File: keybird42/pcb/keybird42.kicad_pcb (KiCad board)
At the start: 2 copper layers, 420.3 x 95.2 mm, 176 parts, among them SW111 SW_MX, SW112 SW_MX, SW113 SW_MX, SW114 SW_MX, SW115 SW_MX, SW116 SW_MX, SW117 SW_MX, SW121 SW_MX, SW122 SW_MX, SW123 SW_MX, SW124 SW_MX, SW125 SW_MX, SW126 SW_MX, SW127 SW_MX, SW131 SW_MX, SW132 SW_MX, SW133 SW_MX, SW134 SW_MX, SW135 SW_MX, SW136 SW_MX, SW137 SW_MX, SW211 SW_MX, SW212 SW_MX, SW213 SW_MX, SW214 SW_MX, SW215 SW_MX, SW216 SW_MX, SW217 SW_MX, SW221 SW_MX, SW222 SW_MX, SW223 SW_MX, SW225 SW_MX, SW226 SW_MX, SW227 SW_MX, SW231 SW_MX, SW232 SW_MX, SW233 SW_MX, SW234 SW_MX, SW235 SW_MX, SW236 SW_MX, SW237 SW_MX, SW311 SW_MX, SW312 SW_MX, SW314 SW_MX, SW315 SW_MX, SW316 SW_MX, SW317 SW_MX, SW321 SW_MX, SW322 SW_MX, SW323 SW_MX, SW324 SW_MX, SW325 SW_MX, SW327 SW_MX, SW331 SW_MX, SW332 SW_MX, SW333 SW_MX, SW334 SW_MX, SW335 SW_MX, SW336 SW_MX, SW337 SW_MX, SW411 SW_MX, SW412 SW_MX, SW413 SW_MX, SW414 SW_MX, SW415 SW_MX, SW416 SW_MX, SW417 SW_MX, SW421 SW_MX, SW423 SW_MX, SW424 SW_MX, SW425 SW_MX, SW426 SW_MX, SW427 SW_MX, SW431 SW_MX, SW432 SW_MX, SW433 SW_MX, SW434 SW_MX, SW436 SW_MX, SW437 SW_MX, SW501 SW_MX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

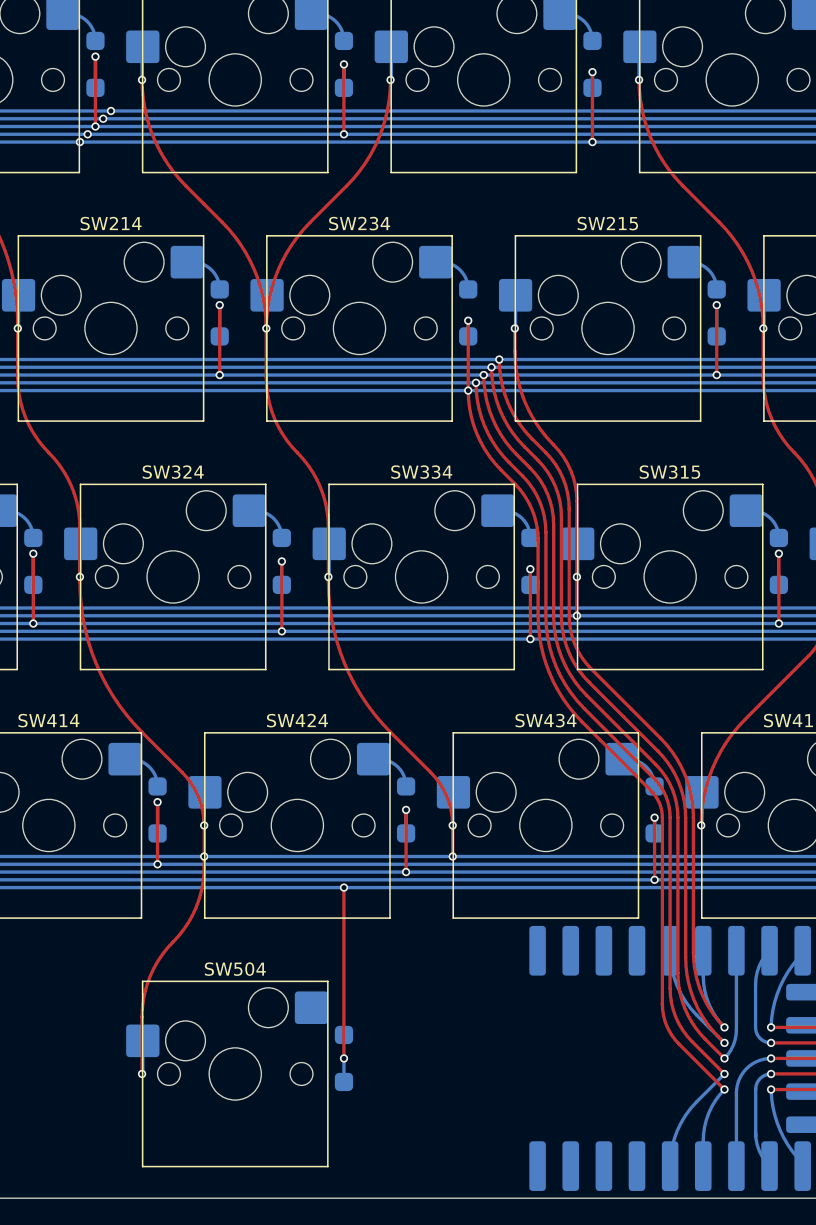
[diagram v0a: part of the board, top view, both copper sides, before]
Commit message: more vertical bus layout
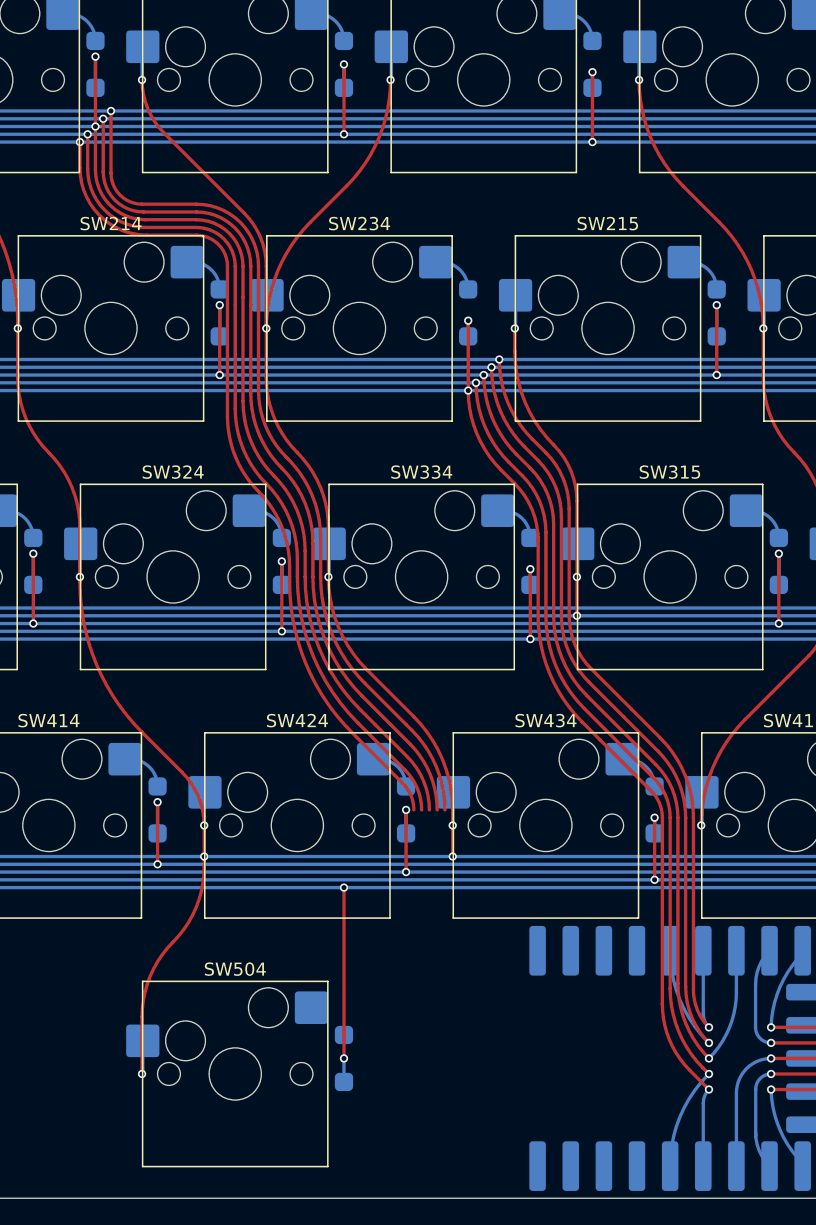
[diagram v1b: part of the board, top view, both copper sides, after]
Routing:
- net /COL1: track 714.5 -> 780.2 mm
- net /COL7: track 661.9 -> 726.9 mm
- net /ROW11: track 464.9 -> 529.3 mm
- net /ROW12: track 460.7 -> 524.5 mm
- net /ROW13: track 456.5 -> 519.7 mm
- net /ROW22: track 521.2 -> 519.9 mm
- net /COL6: track 716.6 -> 715.6 mm
- net /ROW23: track 522.9 -> 522.0 mm
- net /COL4: track 683.8 -> 684.4 mm
- net /COL2: track 726.6 -> 726.1 mm

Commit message: routing done?
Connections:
- U1 pad 1: /ROW12 -> /COL1
- U1 pad 17: /ROW23 -> /ROW21
- U1 pad 18: /ROW22 -> /ROW23
- U1 pad 19: /COL7 -> /ROW13
- U1 pad 2: /ROW13 -> /COL7
- U1 pad 3: /ROW21 -> /ROW12
- U1 pad 4: /COL6 -> /ROW22
- U1 pad 5: /COL2 -> /COL6
- U1 pad 6: /ROW21 -> /COL2
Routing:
- net /ROW12: track 524.5 -> 561.8 mm, vias 15 -> 16
- net /ROW13: track 519.7 -> 556.1 mm, vias 15 -> 16
- net /ROW11: track 529.3 -> 563.8 mm, vias 14 -> 15
- net /COL7: track 726.9 -> 758.2 mm, vias 17 -> 18
- net /COL1: track 780.2 -> 808.7 mm, vias 15 -> 16
- net /COL2: track 726.1 -> 729.6 mm
- net /ROW21: track 531.4 -> 530.8 mm

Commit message: starting to fix DRC complaints
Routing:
- net /COL4: track 684.4 -> 679.6 mm
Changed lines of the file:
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@@
   (segment (start 226.21894 88.106324) (end 226.21894 88.905917) (width 0.254) (layer "F.Cu") (net 103))
   (segment (start 221.456436 100.403617) (end 221.456436 104.775088) (width 0.254) (layer "F.Cu") (net 103))
+  (segment (start 226.21894 35.71878) (end 229.718594 39.218434) (width 0.254) (layer "F.Cu") (net 103))
   (segment (start 197.643916 66.675056) (end 197.643916 67.083615) (width 0.254) (layer "F.Cu") (net 103))
-  (segment (start 237.138853 36.705127) (end 234.349043 39.494937) (width 0.254) (layer "F.Cu") (net 103))
+  (segment (start 223.140235 32.640076) (end 226.21894 35.71878) (width 0.254) (layer "F.Cu") (net 103))
   (segment (start 204.090219 32.640076) (end 207.168924 35.71878) (width 0.254) (layer "F.Cu") (net 103))
+  (segment (start 230.981444 42.267223) (end 230.981444 47.62504) (width 0.254) (layer "F.Cu") (net 103))
+  (segment (start 235.743948 35.71878) (end 232.244294 39.218434) (width 0.254) (layer "F.Cu") (net 103))
   (segment (start 226.21894 85.725072) (end 226.21894 88.106324) (width 0.254) (layer "F.Cu") (net 103))
   (segment (start 235.743948 62.898594) (end 235.743948 66.675056) (width 0.254) (layer "F.Cu") (net 103))
-  (segment (start 230.981444 42.862536) (end 230.981444 47.62504) (width 0.254) (layer "F.Cu") (net 103))
   (segment (start 216.693932 62.898898) (end 216.693932 66.675056) (width 0.254) (layer "F.Cu") (net 103))
   (segment (start 221.456436 78.581316) (end 224.53514 81.66002) (width 0.254) (layer "F.Cu") (net 103))
-  (segment (start 226.21894 35.71878) (end 229.297644 38.797484) (width 0.254) (layer "F.Cu") (net 103))
+  (segment (start 238.822653 32.640076) (end 235.743948 35.71878) (width 0.254) (layer "F.Cu") (net 103))
   (segment (start 211.931428 47.62504) (end 211.931428 51.401198) (width 0.254) (layer "F.Cu") (net 103))
-  (segment (start 223.140235 32.640076) (end 226.21894 35.71878) (width 0.254) (layer "F.Cu") (net 103))
   (segment (start 238.690597 73.788896) (end 242.292391 77.39069) (width 0.254) (layer "F.Cu") (net 103))
   (via (at 216.693932 66.675056) (size 0.635) (drill 0.381) (layers "F.Cu" "B.Cu") (net 103))
@@
   (via (at 245.268956 85.725072) (size 0.635) (drill 0.381) (layers "F.Cu" "B.Cu") (net 103))
   (arc (start 207.168924 35.71878) (mid 210.693693 40.99397) (end 211.931428 47.216481) (width 0.254) (layer "F.Cu") (net 103))
-  (arc (start 240.506452 28.575024) (mid 239.631242 32.975004) (end 237.138853 36.705127) (width 0.254) (layer "F.Cu") (net 103))
+  (arc (start 229.718594 39.218434) (mid 230.653239 40.61723) (end 230.981444 42.267223) (width 0.254) (layer "F.Cu") (net 103))
   (arc (start 233.362696 57.150048) (mid 235.125102 59.787537) (end 235.743948 62.898594) (width 0.254) (layer "F.Cu") (net 103))
   (arc (start 242.292391 77.39069) (mid 244.495371 80.687684) (end 245.268956 84.576753) (width 0.254) (layer "F.Cu") (net 103))
   (arc (start 205.485124 81.66002) (mid 206.731319 83.525081) (end 207.168924 85.725072) (width 0.254) (layer "F.Cu") (net 103))
-  (arc (start 221.456436 28.575024) (mid 221.894041 30.775014) (end 223.140235 32.640076) (width 0.254) (layer "F.Cu") (net 103))
   (arc (start 214.31268 57.150048) (mid 216.075065 59.787642) (end 216.693932 62.898898) (width 0.254) (layer "F.Cu") (net 103))
-  (arc (start 234.349043 39.494937) (mid 231.856654 43.22506) (end 230.981444 47.62504) (width 0.254) (layer "F.Cu") (net 103))
   (arc (start 226.21894 88.905917) (mid 225.600073 92.017172) (end 223.837688 94.654767) (width 0.254) (layer "F.Cu") (net 103))
   (arc (start 223.837688 94.654767) (mid 222.075303 97.292361) (end 221.456436 100.403617) (width 0.254) (layer "F.Cu") (net 103))
   (arc (start 224.53514 81.66002) (mid 225.781335 83.525081) (end 226.21894 85.725072) (width 0.254) (layer "F.Cu") (net 103))
   (arc (start 202.40642 28.575024) (mid 202.844025 30.775014) (end 204.090219 32.640076) (width 0.254) (layer "F.Cu") (net 103))
-  (arc (start 229.297644 38.797484) (mid 230.543839 40.662545) (end 230.981444 42.862536) (width 0.254) (layer "F.Cu") (net 103))
   (arc (start 216.693932 67.083615) (mid 217.931666 73.306126) (end 221.456436 78.581316) (width 0.254) (layer "F.Cu") (net 103))
+  (arc (start 240.506452 28.575024) (mid 240.068847 30.775014) (end 238.822653 32.640076) (width 0.254) (layer "F.Cu") (net 103))
+  (arc (start 221.456436 28.575024) (mid 221.894041 30.775014) (end 223.140235 32.640076) (width 0.254) (layer "F.Cu") (net 103))
   (arc (start 230.981444 51.401198) (mid 231.600311 54.512453) (end 233.362696 57.150048) (width 0.254) (layer "F.Cu") (net 103))
   (arc (start 235.743948 66.675056) (mid 236.509757 70.525038) (end 238.690597 73.788896) (width 0.254) (layer "F.Cu") (net 103))
   (arc (start 211.931428 51.401198) (mid 212.550295 54.512453) (end 214.31268 57.150048) (width 0.254) (layer "F.Cu") (net 103))
+  (arc (start 232.244294 39.218434) (mid 231.309648 40.61723) (end 230.981444 42.267223) (width 0.254) (layer "F.Cu") (net 103))
   (arc (start 197.643916 67.083615) (mid 198.88165 73.306126) (end 202.40642 78.581316) (width 0.254) (layer "F.Cu") (net 103))
   (segment (start 207.22768 83.185072) (end 207.22768 85.666316) (width 0.254) (layer "B.Cu") (net 103))
@@
   (arc (start 377.428442 97.631332) (mid 375.778449 97.303128) (end 374.379653 96.368482) (width 0.254) (layer "B.Cu") (net 103))
   (arc (start 207.22768 85.666316) (mid 207.210471 85.707863) (end 207.168924 85.725072) (width 0.254) (layer "B.Cu") (net 103))
-  (arc (start 230.981444 45.226366) (mid 230.996662 45.14986) (end 231.04 45.085) (width 0.254) (layer "B.Cu") (net 103))
   (segment (start 297.686416 78.611232) (end 296.261595 77.186411) (width 0.254) (layer "F.Cu") (net 104))
   (segment (start 288.131492 47.62504) (end 288.131492 52.83841) (width 0.254) (layer "F.Cu") (net 104))

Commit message: reduce silkscreen clutter
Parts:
- removed REF** (x2): Stabilizer_Cherry_MX_2.00u, PCM_Mounting_Keyboard_Stabilizer:Stabilizer_Cherry_MX_2.00u
- removed REF**: Stabilizer_Cherry_MX_7.00u, PCM_Mounting_Keyboard_Stabilizer:Stabilizer_Cherry_MX_7.00u
- SW111, SW112, SW113, SW114, SW115, SW116, SW117, SW121, SW122, SW123, SW124, SW125, SW126, SW127, SW131, SW132, SW133, SW134, SW135, SW136, SW137, SW211, SW212, SW213, SW214, SW215, SW216, SW217, SW221, SW222, SW223, SW225, SW226, SW227, SW231, SW232, SW233, SW234, SW235, SW236, SW237, SW311, SW312, SW314, SW315, SW316, SW317, SW321, SW322, SW323, SW324, SW325, SW327, SW331, SW332, SW333, SW334, SW335, SW336, SW337, SW411, SW412, SW413, SW414, SW415, SW416, SW417, SW421, SW423, SW424, SW425, SW426, SW427, SW431, SW432, SW433, SW434, SW436, SW437, SW501, SW502, SW503, SW504, SW505, SW506, SW507: footprint PCM_Switch_Keyboard_Hotswap_Kailh:SW_Hotswap_Kailh_MX -> keybird42:SW_Hotswap_Kailh_MX
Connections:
- U1 pad 1: /COL1 -> /ROW12
- U1 pad 10: /ROW41 -> /ROW42
- U1 pad 11: /ROW42 -> /ROW43
- U1 pad 12: /ROW43 -> /ROW50
- U1 pad 13: /ROW50 -> /COL1
- U1 pad 14: /COL3 -> /COL2
- U1 pad 15: /COL5 -> /COL3
- U1 pad 16: /ROW31 -> /COL4
- U1 pad 17: /ROW21 -> /COL5
- U1 pad 18: /ROW23 -> /COL6
- U1 pad 19: /ROW13 -> /COL7
- U1 pad 2: /COL7 -> /ROW13
- U1 pad 3: /ROW12 -> /ROW21
- U1 pad 5: /COL6 -> /ROW23
- U1 pad 6: /COL2 -> /ROW31
- U1 pad 9: /COL4 -> /ROW41

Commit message: whoops, lost the stabs
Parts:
- added REF**: Stabilizer_Cherry_MX_7.00u, PCM_Mounting_Keyboard_Stabilizer:Stabilizer_Cherry_MX_7.00u, F.Cu at (228.6, 104.8)
- added REF**: Stabilizer_Cherry_MX_2.00u, PCM_Mounting_Keyboard_Stabilizer:Stabilizer_Cherry_MX_2.00u, F.Cu at (107.2, 85.7)
- added REF**: Stabilizer_Cherry_MX_2.00u, PCM_Mounting_Keyboard_Stabilizer:Stabilizer_Cherry_MX_2.00u, F.Cu at (350.0, 66.7)
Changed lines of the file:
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@@
     )
   )
+  (footprint "PCM_Mounting_Keyboard_Stabilizer:Stabilizer_Cherry_MX_7.00u" (layer "F.Cu")
+    (at 228.600192 104.775088 180)
+    (descr "Cherry MX PCB Stabilizer 7.00u")
+    (tags "Cherry MX Keyboard Stabilizer 7.00u Cutout")
+    (attr exclude_from_pos_files exclude_from_bom)
+    (fp_text reference "REF**" (at 0 -3.4) (layer "F.Fab") hide
+        (effects (font (size 1 1) (thickness 0.15)))
+    )
+    (fp_text value "Stabilizer_Cherry_MX_7.00u" (at 0 3.4) (layer "F.Fab") hide
+        (effects (font (size 1 1) (thickness 0.15)))
+    )
+    (fp_line (start -2 0) (end 2 0)
+      (stroke (width 0.1) (type solid)) (layer "Dwgs.User"))
+    (fp_line (start 0 2) (end 0 -2)
+      (stroke (width 0.1) (type solid)) (layer "Dwgs.User"))
+    (fp_line (start -60.525 -5.53) (end -60.525 6.77)
+      (stroke (width 0.1) (type solid)) (layer "Eco1.User"))
+    (fp_line (start -60.525 6.77) (end -53.775 6.77)
+      (stroke (width 0.1) (type solid)) (layer "Eco1.User"))
+    (fp_line (start -53.775 -5.53) (end -60.525 -5.53)
+      (stroke (width 0.1) (type solid)) (layer "Eco1.User"))
+    (fp_line (start -53.775 6.77) (end -53.775 -5.53)
+      (stroke (width 0.1) (type solid)) (layer "Eco1.User"))
+    (fp_line (start 53.775 -5.53) (end 53.775 6.77)
+      (stroke (width 0.1) (type solid)) (layer "Eco1.User"))
+    (fp_line (start 53.775 6.77) (end 60.525 6.77)
+      (stroke (width 0.1) (type solid)) (layer "Eco1.User"))
+    (fp_line (start 60.525 -5.53) (end 53.775 -5.53)
+      (stroke (width 0.1) (type solid)) (layer "Eco1.User"))
+    (fp_line (start 60.525 6.77) (end 60.525 -5.53)
+      (stroke (width 0.1) (type solid)) (layer "Eco1.User"))
+    (pad "" np_thru_hole circle (at -57.15 -6.985 180) (size 3.048 3.048) (drill 3.048) (layers "*.Cu" "*.Mask"))
+    (pad "" np_thru_hole circle (at -57.15 8.225 180) (size 3.9878 3.9878) (drill 3.9878) (layers "*.Cu" "*.Mask"))
+    (pad "" np_thru_hole circle (at 57.15 -6.985 180) (size 3.048 3.048) (drill 3.048) (layers "*.Cu" "*.Mask"))
+    (pad "" np_thru_hole circle (at 57.15 8.225 180) (size 3.9878 3.9878) (drill 3.9878) (layers "*.Cu" "*.Mask"))
+    (model "${KICAD6_3RD_PARTY}/3dmodels/com_github_perigoso_keyswitch-kicad-library/3d-library.3dshapes/Stabilizer_Cherry_MX_7.00u.wrl"
+      (offset (xyz 0 0 0))
+      (scale (xyz 1 1 1))
+      (rotate (xyz 0 0 0))
+    )
+  )
   (footprint "keybird42:SW_Hotswap_Kailh_MX" (layer "F.Cu")
     (at 404.8125 52.3875)
@@
     )
   )
+  (footprint "PCM_Mounting_Keyboard_Stabilizer:Stabilizer_Cherry_MX_2.00u" (layer "F.Cu")
+    (at 107.15634 85.725072 180)
+    (descr "Cherry MX PCB Stabilizer 2.00u 2.25u 2.50u 2.75u")
+    (tags "Cherry MX Keyboard Stabilizer 2.00u 2.25u 2.50u 2.75u Cutout")
+    (attr exclude_from_pos_files exclude_from_bom)
+    (fp_text reference "REF**" (at 0 -3.4) (layer "F.Fab") hide
+        (effects (font (size 1 1) (thickness 0.15)))
+    )
+    (fp_text value "Stabilizer_Cherry_MX_2.00u" (at 0 3.6) (layer "F.Fab") hide
+        (effects (font (size 1 1) (thickness 0.15)))
+    )
+    (fp_line (start -2 0) (end 2 0)
+      (stroke (width 0.1) (type solid)) (layer "Dwgs.User"))
+    (fp_line (start 0 2) (end 0 -2)
+      (stroke (width 0.1) (type solid)) (layer "Dwgs.User"))
+    (fp_line (start -15.313 -5.53) (end -15.313 6.77)
+      (stroke (width 0.1) (type solid)) (layer "Eco1.User"))
+    (fp_line (start -15.313 6.77) (end -8.563 6.77)
+      (stroke (width 0.1) (type solid)) (layer "Eco1.User"))
+    (fp_line (start -8.563 -5.53) (end -15.313 -5.53)
+      (stroke (width 0.1) (type solid)) (layer "Eco1.User"))
+    (fp_line (start -8.563 6.77) (end -8.563 -5.53)
+      (stroke (width 0.1) (type solid)) (layer "Eco1.User"))
+    (fp_line (start 8.563 -5.53) (end 8.563 6.77)
+      (stroke (width 0.1) (type solid)) (layer "Eco1.User"))
+    (fp_line (start 8.563 6.77) (end 15.313 6.77)
+      (stroke (width 0.1) (type solid)) (layer "Eco1.User"))
+    (fp_line (start 15.313 -5.53) (end 8.563 -5.53)
+      (stroke (width 0.1) (type solid)) (layer "Eco1.User"))
+    (fp_line (start 15.313 6.77) (end 15.313 -5.53)
+      (stroke (width 0.1) (type solid)) (layer "Eco1.User"))
+    (pad "" np_thru_hole circle (at -11.938 -6.985 180) (size 3.048 3.048) (drill 3.048) (layers "*.Cu" "*.Mask"))
+    (pad "" np_thru_hole circle (at -11.938 8.225 180) (size 3.9878 3.9878) (drill 3.9878) (layers "*.Cu" "*.Mask"))
+    (pad "" np_thru_hole circle (at 11.938 -6.985 180) (size 3.048 3.048) (drill 3.048) (layers "*.Cu" "*.Mask"))
+    (pad "" np_thru_hole circle (at 11.938 8.225 180) (size 3.9878 3.9878) (drill 3.9878) (layers "*.Cu" "*.Mask"))
+    (model "${KICAD6_3RD_PARTY}/3dmodels/com_github_perigoso_keyswitch-kicad-library/3d-library.3dshapes/Stabilizer_Cherry_MX_2.00u.wrl"
+      (offset (xyz 0 0 0))
+      (scale (xyz 1 1 1))
+      (rotate (xyz 0 0 0))
+    )
+  )
   (footprint "keybird42:SW_Hotswap_Kailh_MX" (layer "F.Cu")
     (at 385.762824 33.3375)
@@
       (net 11 "Net-(D122-A)") (pinfunction "A") (pintype "passive"))
   )
+  (footprint "PCM_Mounting_Keyboard_Stabilizer:Stabilizer_Cherry_MX_2.00u" (layer "F.Cu")
+    (at 350.044044 66.675056 180)
+    (descr "Cherry MX PCB Stabilizer 2.00u 2.25u 2.50u 2.75u")
+    (tags "Cherry MX Keyboard Stabilizer 2.00u 2.25u 2.50u 2.75u Cutout")
+    (attr exclude_from_pos_files exclude_from_bom)
+    (fp_text reference "REF**" (at 0 -3.4) (layer "F.Fab") hide
+        (effects (font (size 1 1) (thickness 0.15)))
+    )
+    (fp_text value "Stabilizer_Cherry_MX_2.00u" (at 0 3.6) (layer "F.Fab") hide
+        (effects (font (size 1 1) (thickness 0.15)))
+    )
+    (fp_line (start -2 0) (end 2 0)
+      (stroke (width 0.1) (type solid)) (layer "Dwgs.User"))
+    (fp_line (start 0 2) (end 0 -2)
+      (stroke (width 0.1) (type solid)) (layer "Dwgs.User"))
+    (fp_line (start -15.313 -5.53) (end -15.313 6.77)
+      (stroke (width 0.1) (type solid)) (layer "Eco1.User"))
+    (fp_line (start -15.313 6.77) (end -8.563 6.77)
+      (stroke (width 0.1) (type solid)) (layer "Eco1.User"))
+    (fp_line (start -8.563 -5.53) (end -15.313 -5.53)
+      (stroke (width 0.1) (type solid)) (layer "Eco1.User"))
+    (fp_line (start -8.563 6.77) (end -8.563 -5.53)
+      (stroke (width 0.1) (type solid)) (layer "Eco1.User"))
+    (fp_line (start 8.563 -5.53) (end 8.563 6.77)
+      (stroke (width 0.1) (type solid)) (layer "Eco1.User"))
+    (fp_line (start 8.563 6.77) (end 15.313 6.77)
+      (stroke (width 0.1) (type solid)) (layer "Eco1.User"))
+    (fp_line (start 15.313 -5.53) (end 8.563 -5.53)
+      (stroke (width 0.1) (type solid)) (layer "Eco1.User"))
+    (fp_line (start 15.313 6.77) (end 15.313 -5.53)
+      (stroke (width 0.1) (type solid)) (layer "Eco1.User"))
+    (pad "" np_thru_hole circle (at -11.938 -6.985 180) (size 3.048 3.048) (drill 3.048) (layers "F&B.Cu" "*.Mask"))
+    (pad "" np_thru_hole circle (at -11.938 8.225 180) (size 3.9878 3.9878) (drill 3.9878) (layers "F&B.Cu" "*.Mask"))
+    (pad "" np_thru_hole circle (at 11.938 -6.985 180) (size 3.048 3.048) (drill 3.048) (layers "F&B.Cu" "*.Mask"))
+    (pad "" np_thru_hole circle (at 11.938 8.225 180) (size 3.9878 3.9878) (drill 3.9878) (layers "F&B.Cu" "*.Mask"))
+    (model "${KICAD6_3RD_PARTY}/3dmodels/com_github_perigoso_keyswitch-kicad-library/3d-library.3dshapes/Stabilizer_Cherry_MX_2.00u.wrl"
+      (offset (xyz 0 0 0))
+      (scale (xyz 1 1 1))
+      (rotate (xyz 0 0 0))
+    )
+  )
   (footprint "keybird42:SW_Hotswap_Kailh_MX" (layer "F.Cu")
